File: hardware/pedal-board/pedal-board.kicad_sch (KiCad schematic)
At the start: 43 parts, among them J1 AudioJack0, J12 Qwiic, J13 Qwiic, J2 AudioJack1, J3 AudioJack2, J4 AudioJack3, J5 Qwiic, J6 IRQ, J7 Serial Wire Debug, Q1 Q_NPN_BEC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

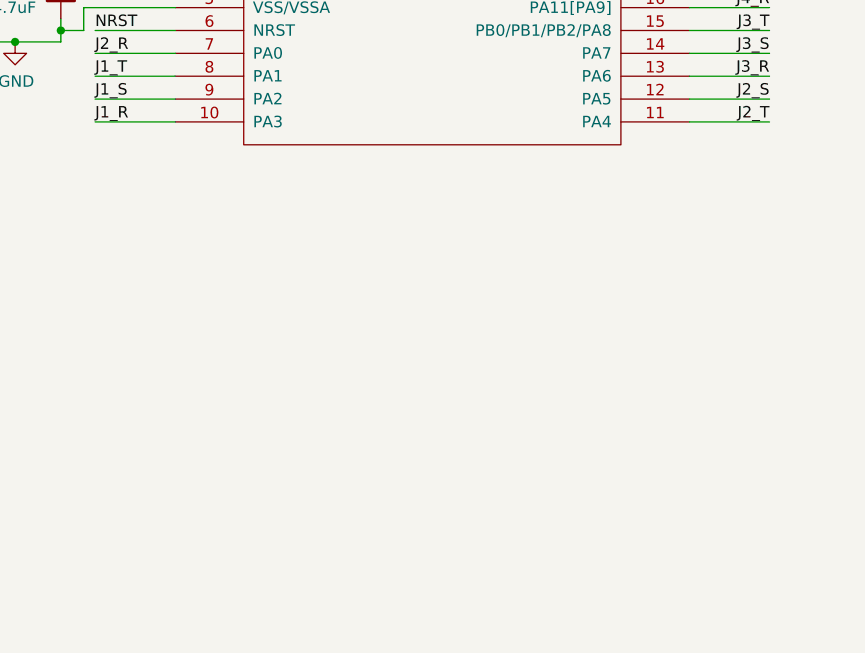
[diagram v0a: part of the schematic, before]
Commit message: Brought out all ADC lines, and put some power on adjacent pins
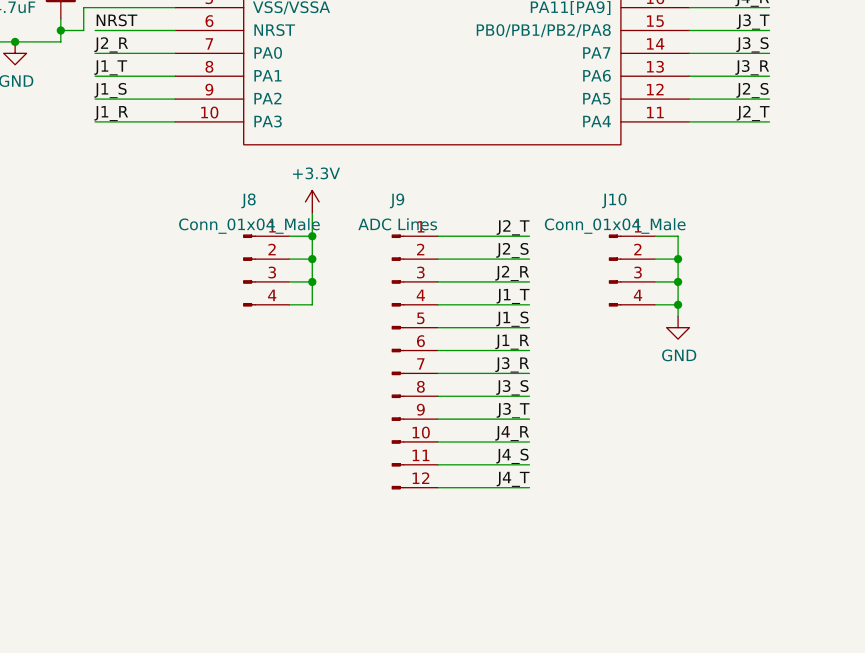
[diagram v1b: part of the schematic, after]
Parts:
- added J10, J8: Conn_01x04_Male, Connector_PinHeader_2.54mm:PinHeader_1x04_P2.54mm_Vertical, symbol Connector:Conn_01x04_Male
- added J9: ADC Lines, Connector_PinHeader_2.54mm:PinHeader_1x12_P2.54mm_Vertical, symbol Connector:Conn_01x12_Male
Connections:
- net +3V3: now also J8.1 (Pin_1), J8.2 (Pin_2), J8.3 (Pin_3), J8.4 (Pin_4)
- net GND: now also J10.1 (Pin_1), J10.2 (Pin_2), J10.3 (Pin_3), J10.4 (Pin_4)
- net J1_R: now also J9.6 (Pin_6)
- net J1_S: now also J9.5 (Pin_5)
- net J1_T: now also J9.4 (Pin_4)
- net J2_R: now also J9.3 (Pin_3)
- net J2_S: now also J9.2 (Pin_2)
- net J2_T: now also J9.1 (Pin_1)
- net J3_R: now also J9.7 (Pin_7)
- net J3_S: now also J9.8 (Pin_8)
- net J3_T: now also J9.9 (Pin_9)
- net J4_R: now also J9.10 (Pin_10)
- net J4_S: now also J9.11 (Pin_11)
- net J4_T: now also J9.12 (Pin_12)

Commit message: Convert all other mounting holes to non-pad variety.
Reroute a few traces to be shorter.
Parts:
- H1, H2, H3: footprint Mounting_Holes:MountingHole_3.2mm_M3_Pad_Via -> MountingHole:MountingHole_3.2mm_M3; symbol Mechanical:MountingHole_Pad -> Mechanical:MountingHole
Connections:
- net GND: no longer H1.1, H2.1, H3.1
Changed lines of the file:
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@@
   (junction (at 43.18 27.94) (diameter 0) (color 0 0 0 0)
   )
-  (junction (at 29.21 186.69) (diameter 0) (color 0 0 0 0)
-  )
   (junction (at 55.88 22.86) (diameter 0) (color 0 0 0 0)
   )
@@
     (stroke (width 0) (type default) (color 0 0 0 0))
   )
-  (wire (pts (xy 29.21 186.69) (xy 29.21 187.96))
-    (stroke (width 0) (type default) (color 0 0 0 0))
-  )
   (wire (pts (xy 204.47 124.46) (xy 212.09 124.46))
     (stroke (width 0) (type default) (color 0 0 0 0))
@@
     (stroke (width 0) (type default) (color 0 0 0 0))
   )
-  (wire (pts (xy 29.21 185.42) (xy 29.21 186.69))
-    (stroke (width 0) (type default) (color 0 0 0 0))
-  )
   (wire (pts (xy 49.53 25.4) (xy 49.53 34.29))
     (stroke (width 0) (type default) (color 0 0 0 0))
@@
     (stroke (width 0) (type default) (color 0 0 0 0))
   )
-  (wire (pts (xy 36.83 186.69) (xy 36.83 185.42))
-    (stroke (width 0) (type default) (color 0 0 0 0))
-  )
   (wire (pts (xy 49.53 142.24) (xy 55.88 142.24))
     (stroke (width 0) (type default) (color 0 0 0 0))
@@
     (stroke (width 0) (type default) (color 0 0 0 0))
   )
-  (wire (pts (xy 21.59 185.42) (xy 21.59 186.69))
-    (stroke (width 0) (type default) (color 0 0 0 0))
-  )
   (wire (pts (xy 133.35 102.87) (xy 143.51 102.87))
     (stroke (width 0) (type default) (color 0 0 0 0))
@@
     (stroke (width 0) (type default) (color 0 0 0 0))
   )
-  (wire (pts (xy 21.59 186.69) (xy 29.21 186.69))
-    (stroke (width 0) (type default) (color 0 0 0 0))
-  )
   (wire (pts (xy 49.53 162.56) (xy 55.88 162.56))
     (stroke (width 0) (type default) (color 0 0 0 0))
@@
   )
   (wire (pts (xy 43.18 83.82) (xy 43.18 85.09))
-    (stroke (width 0) (type default) (color 0 0 0 0))
-  )
-  (wire (pts (xy 29.21 186.69) (xy 36.83 186.69))
     (stroke (width 0) (type default) (color 0 0 0 0))
   )
@@
     (pin "1")
   )
-  (symbol (lib_id "Mechanical:MountingHole_Pad") (at 21.59 182.88 0) (unit 1)
+  (symbol (lib_id "Mechanical:MountingHole") (at 21.59 182.88 0) (unit 1)
     (in_bom yes) (on_board yes)
     (property "Reference" "H1" (id 0) (at 24.13 181.6354 0)
@@
       (effects (font (size 1.27 1.27)) (justify left))
     )
-    (property "Footprint" "Mounting_Holes:MountingHole_3.2mm_M3_Pad_Via" (id 2) (at 21.59 182.88 0)
+    (property "Footprint" "MountingHole:MountingHole_3.2mm_M3" (id 2) (at 21.59 182.88 0)
       (effects (font (size 1.27 1.27)) hide)
     )
@@
       (effects (font (size 1.27 1.27)) hide)
     )
-    (pin "1")
-  )
-  (symbol (lib_id "Mechanical:MountingHole_Pad") (at 29.21 182.88 0) (unit 1)
+  )
+  (symbol (lib_id "Mechanical:MountingHole") (at 29.21 182.88 0) (unit 1)
     (in_bom yes) (on_board yes)
     (property "Reference" "H2" (id 0) (at 31.75 181.6354 0)
@@
       (effects (font (size 1.27 1.27)) (justify left))
     )
-    (property "Footprint" "Mounting_Holes:MountingHole_3.2mm_M3_Pad_Via" (id 2) (at 29.21 182.88 0)
+    (property "Footprint" "MountingHole:MountingHole_3.2mm_M3" (id 2) (at 29.21 182.88 0)
       (effects (font (size 1.27 1.27)) hide)
     )
@@
       (effects (font (size 1.27 1.27)) hide)
     )
-    (pin "1")
-  )
-  (symbol (lib_id "Mechanical:MountingHole_Pad") (at 36.83 182.88 0) (unit 1)
+  )
+  (symbol (lib_id "Mechanical:MountingHole") (at 36.83 182.88 0) (unit 1)
     (in_bom yes) (on_board yes)
     (property "Reference" "H3" (id 0) (at 39.37 181.6354 0)
@@
       (effects (font (size 1.27 1.27)) (justify left))
     )
-    (property "Footprint" "Mounting_Holes:MountingHole_3.2mm_M3_Pad_Via" (id 2) (at 36.83 182.88 0)
+    (property "Footprint" "MountingHole:MountingHole_3.2mm_M3" (id 2) (at 36.83 182.88 0)
       (effects (font (size 1.27 1.27)) hide)
     )
@@
       (effects (font (size 1.27 1.27)) hide)
     )
-    (pin "1")
-  )
-  (symbol (lib_id "power:GND") (at 29.21 187.96 0) (unit 1)
-    (in_bom yes) (on_board yes)
-    (property "Reference" "#PWR0122" (id 0) (at 29.21 194.31 0)
-      (effects (font (size 1.27 1.27)) hide)
-    )
-    (property "Value" "GND" (id 1) (at 29.337 192.3542 0))
-    (property "Footprint" "" (id 2) (at 29.21 187.96 0)
-      (effects (font (size 1.27 1.27)) hide)
-    )
-    (property "Datasheet" "" (id 3) (at 29.21 187.96 0)
-      (effects (font (size 1.27 1.27)) hide)
-    )
-    (pin "1")
   )
   (symbol (lib_id "Connector:Conn_01x04_Female") (at 215.9 63.5 0) (mirror x) (unit 1)
@@
       (reference "#PWR0121") (unit 1) (value "GND") (footprint "")
     )
-    (path "/00000000-0000-0000-0000-000060091cc7"
-      (reference "#PWR0122") (unit 1) (value "GND") (footprint "")
-    )
     (path "/00000000-0000-0000-0000-0000600d3c6e"
       (reference "#PWR0123") (unit 1) (value "+3.3V") (footprint "")
@@
     )
     (path "/00000000-0000-0000-0000-0000600874db"
-      (reference "H1") (unit 1) (value "MountingHole_Pad") (footprint "Mounting_Holes:MountingHole_3.2mm_M3_Pad_Via")
+      (reference "H1") (unit 1) (value "MountingHole_Pad") (footprint "MountingHole:MountingHole_3.2mm_M3")
     )
     (path "/00000000-0000-0000-0000-000060088095"
-      (reference "H2") (unit 1) (value "MountingHole_Pad") (footprint "Mounting_Holes:MountingHole_3.2mm_M3_Pad_Via")
+      (reference "H2") (unit 1) (value "MountingHole_Pad") (footprint "MountingHole:MountingHole_3.2mm_M3")
     )
     (path "/00000000-0000-0000-0000-0000600884e7"
-      (reference "H3") (unit 1) (value "MountingHole_Pad") (footprint "Mounting_Holes:MountingHole_3.2mm_M3_Pad_Via")
+      (reference "H3") (unit 1) (value "MountingHole_Pad") (footprint "MountingHole:MountingHole_3.2mm_M3")
     )
     (path "/00000000-0000-0000-0000-00005fd72390"
